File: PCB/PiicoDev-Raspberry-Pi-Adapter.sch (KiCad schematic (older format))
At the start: 14 parts, among them J1 Raspberry_Pi_2_3, J2 Conn_PiicoDev_socket, J3 Conn_PiicoDev_socket, J4 Conn_PiicoDev_socket, J5 Conn_PiicoDev_socket, J6 Prototyping Header

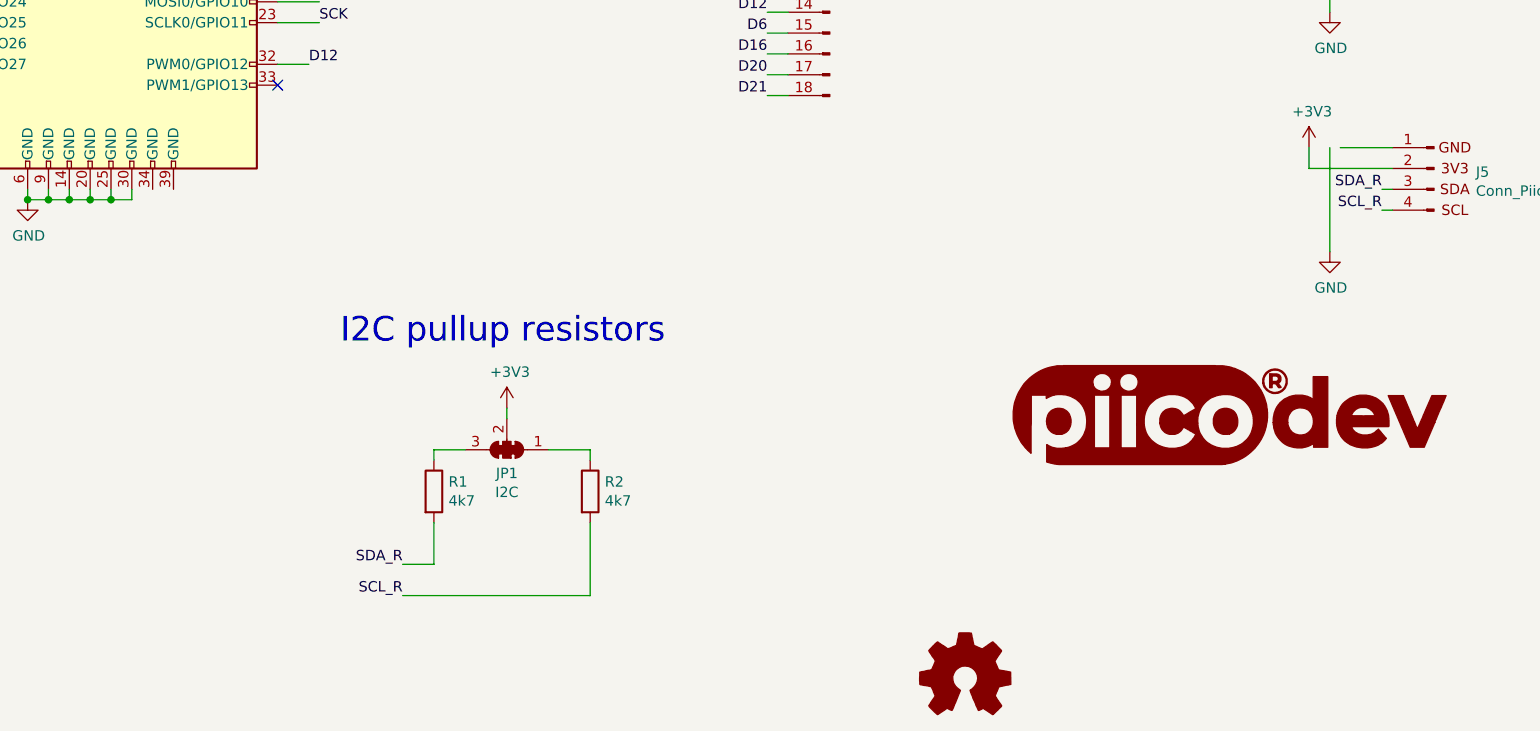
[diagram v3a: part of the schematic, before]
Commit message: v13
Add Raspberry Pi connector pin numbers to silk screen
Update solder jumper with thinner cut trace
Fix PiicoDev connector ground connection
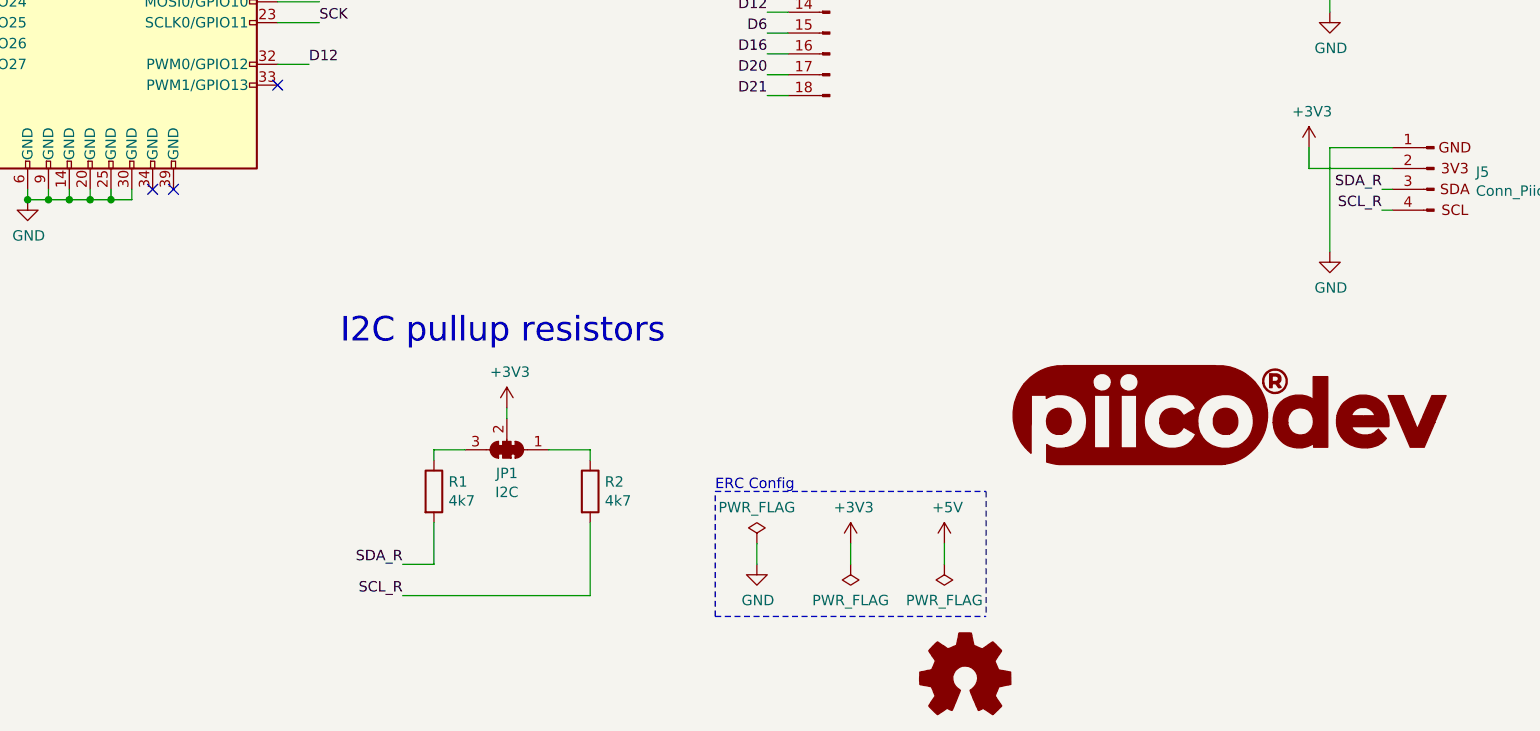
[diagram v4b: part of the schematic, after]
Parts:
- JP1: footprint CoreElectronics_Components:SolderJumper-3_P1.3mm_Closed_RoundedPad1.0x1.5mm -> CoreElectronics_Components:SolderJumper-3_P1.3mm_Closed_RoundedPad1.0x1.5mm_NumberLabels
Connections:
- wire segments 84 -> 87
- no-connect marks 15 -> 17
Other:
- note added: "ERC Config"
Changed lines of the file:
@@
 Sheet 1 1
 Title "PiicoDev Adapter for Raspberry Pi"
-Date "2021-10-29"
-Rev "v12"
+Date "2022-01-18"
+Rev "v13"
 Comp "Core Electronics"
 Comment1 "Based off the design by SparkFun: https://github.com/sparkfun/Qwiic_Hat_for_Raspberry_Pi"
@@
 	1    0    0    -1
 $EndComp
-Wire Wire Line
-	8700 5000 8450 5000
-Wire Wire Line
-	8400 5000 8400 5500
 Wire Wire Line
 	8300 5000 8300 5100
@@
 F 0 "JP1" H 4450 6563 50  0000 C CNN
 F 1 "I2C" H 4450 6654 50  0000 C CNN
-F 2 "CoreElectronics_Components:SolderJumper-3_P1.3mm_Closed_RoundedPad1.0x1.5mm" H 4450 6450 50  0001 C CNN
+F 2 "CoreElectronics_Components:SolderJumper-3_P1.3mm_Closed_RoundedPad1.0x1.5mm_NumberLabels" H 4450 6450 50  0001 C CNN
 F 3 "~" H 4450 6450 50  0001 C CNN
 	1    4450 6450
@@
 Wire Wire Line
 	8400 3850 8700 3850
+$Comp
+L power:PWR_FLAG #FLG0101
+U 1 1 61E658F6
+P 5650 6900
+F 0 "#FLG0101" H 5650 6975 50  0001 C CNN
+F 1 "PWR_FLAG" H 5650 7073 50  0000 C CNN
+F 2 "" H 5650 6900 50  0001 C CNN
+F 3 "~" H 5650 6900 50  0001 C CNN
+	1    5650 6900
+	1    0    0    -1
+$EndComp
+$Comp
+L power:GND #PWR0101
+U 1 1 61E65F24
+P 5650 7000
+F 0 "#PWR0101" H 5650 6750 50  0001 C CNN
+F 1 "GND" H 5655 6827 50  0000 C CNN
+F 2 "" H 5650 7000 50  0001 C CNN
+F 3 "" H 5650 7000 50  0001 C CNN
+	1    5650 7000
+	1    0    0    -1
+$EndComp
+Wire Wire Line
+	5650 6900 5650 7000
+$Comp
+L power:PWR_FLAG #FLG0102
+U 1 1 61E699BD
+P 6100 7000
+F 0 "#FLG0102" H 6100 7075 50  0001 C CNN
+F 1 "PWR_FLAG" H 6100 7173 50  0000 C CNN
+F 2 "" H 6100 7000 50  0001 C CNN
+F 3 "~" H 6100 7000 50  0001 C CNN
+	1    6100 7000
+	-1   0    0    1
+$EndComp
+$Comp
+L power:+3V3 #PWR0102
+U 1 1 61E6AB9F
+P 6100 6900
+F 0 "#PWR0102" H 6100 6750 50  0001 C CNN
+F 1 "+3V3" H 6115 7073 50  0000 C CNN
+F 2 "" H 6100 6900 50  0001 C CNN
+F 3 "" H 6100 6900 50  0001 C CNN
+	1    6100 6900
+	1    0    0    -1
+$EndComp
+Wire Wire Line
+	6100 6900 6100 7000
+Wire Notes Line
+	5450 7250 5450 6650
+Text Notes 5450 6650 0    50   ~ 0
+ERC Config
+$Comp
+L power:PWR_FLAG #FLG0103
+U 1 1 61E743DE
+P 6550 7000
+F 0 "#FLG0103" H 6550 7075 50  0001 C CNN
+F 1 "PWR_FLAG" H 6550 7173 50  0000 C CNN
+F 2 "" H 6550 7000 50  0001 C CNN
+F 3 "~" H 6550 7000 50  0001 C CNN
+	1    6550 7000
+	-1   0    0    1
+$EndComp
+$Comp
+L power:+5V #PWR0103
+U 1 1 61E74F8E
+P 6550 6900
+F 0 "#PWR0103" H 6550 6750 50  0001 C CNN
+F 1 "+5V" H 6565 7073 50  0000 C CNN
+F 2 "" H 6550 6900 50  0001 C CNN
+F 3 "" H 6550 6900 50  0001 C CNN
+	1    6550 6900
+	1    0    0    -1
+$EndComp
+Wire Wire Line
+	6550 6900 6550 7000
+Wire Notes Line
+	6750 6650 6750 7250
+Wire Notes Line
+	5450 6650 6750 6650
+Wire Notes Line
+	5450 7250 6750 7250
+NoConn ~ 2750 5200
+NoConn ~ 2850 5200
+Wire Wire Line
+	8700 5000 8400 5000
+Wire Wire Line
+	8400 5000 8400 5500
 $EndSCHEMATC
